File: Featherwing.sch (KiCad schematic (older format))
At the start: 21 parts, among them J2 CONN_01X16, J3 CONN_01X12, J5 GROVE-CONNECTOR-SMD-90D(4+2P-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, J9 CONN_01X06, U2 ROF-78E

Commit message: Added more signals to JST connector including DMA
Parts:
- J9: footprint Connectors_JST:JST_PH_B6B-PH-SM4-TB_06x2.00mm_Straight -> Connectors_JST:JST_PH_S6B-PH-SM4-TB_06x2.00mm_Angled
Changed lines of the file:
@@
 F 0 "J9" H 3519 3925 50  0000 C CNN
 F 1 "CONN_01X06" H 3519 4016 50  0000 C CNN
-F 2 "Connectors_JST:JST_PH_B6B-PH-SM4-TB_06x2.00mm_Straight" H 0   -150 50  0001 C CNN
+F 2 "Connectors_JST:JST_PH_S6B-PH-SM4-TB_06x2.00mm_Angled" H 0   -150 50  0001 C CNN
 F 3 "" H 0   -150 50  0001 C CNN
 	1    3600 4400

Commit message: Added PM0,1 and Deepsleep circuits
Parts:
- J9: footprint Connectors_JST:JST_PH_S6B-PH-SM4-TB_06x2.00mm_Angled -> Connectors_JST:JST_SH_SM06B-SRSS-TB_06x1.00mm_Angled
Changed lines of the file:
@@
 LIBS:logo
 LIBS:mechanical
+LIBS:whatnick
 LIBS:V9203_Devkit-cache
 EELAYER 26 0
@@
 UC
 $Comp
-L GND #PWR019
+L GND #PWR022
 U 1 1 58E27B40
 P 6800 3500
-F 0 "#PWR019" H 6850 3550 50  0001 C CNN
+F 0 "#PWR022" H 6850 3550 50  0001 C CNN
 F 1 "GND" H 6805 3327 50  0000 C CNN
 F 2 "" H 100 -150 50  0001 C CNN
@@
 $EndComp
 $Comp
-L GND #PWR020
+L GND #PWR023
 U 1 1 58E27FEA
 P 3600 3600
-F 0 "#PWR020" H 3650 3650 50  0001 C CNN
+F 0 "#PWR023" H 3650 3650 50  0001 C CNN
 F 1 "GND" H 3605 3427 50  0000 C CNN
 F 2 "" H -3100 -50 50  0001 C CNN
@@
 F 0 "J9" H 3519 3925 50  0000 C CNN
 F 1 "CONN_01X06" H 3519 4016 50  0000 C CNN
-F 2 "Connectors_JST:JST_PH_S6B-PH-SM4-TB_06x2.00mm_Angled" H 0   -150 50  0001 C CNN
+F 2 "Connectors_JST:JST_SH_SM06B-SRSS-TB_06x1.00mm_Angled" H 0   -150 50  0001 C CNN
 F 3 "" H 0   -150 50  0001 C CNN
 	1    3600 4400

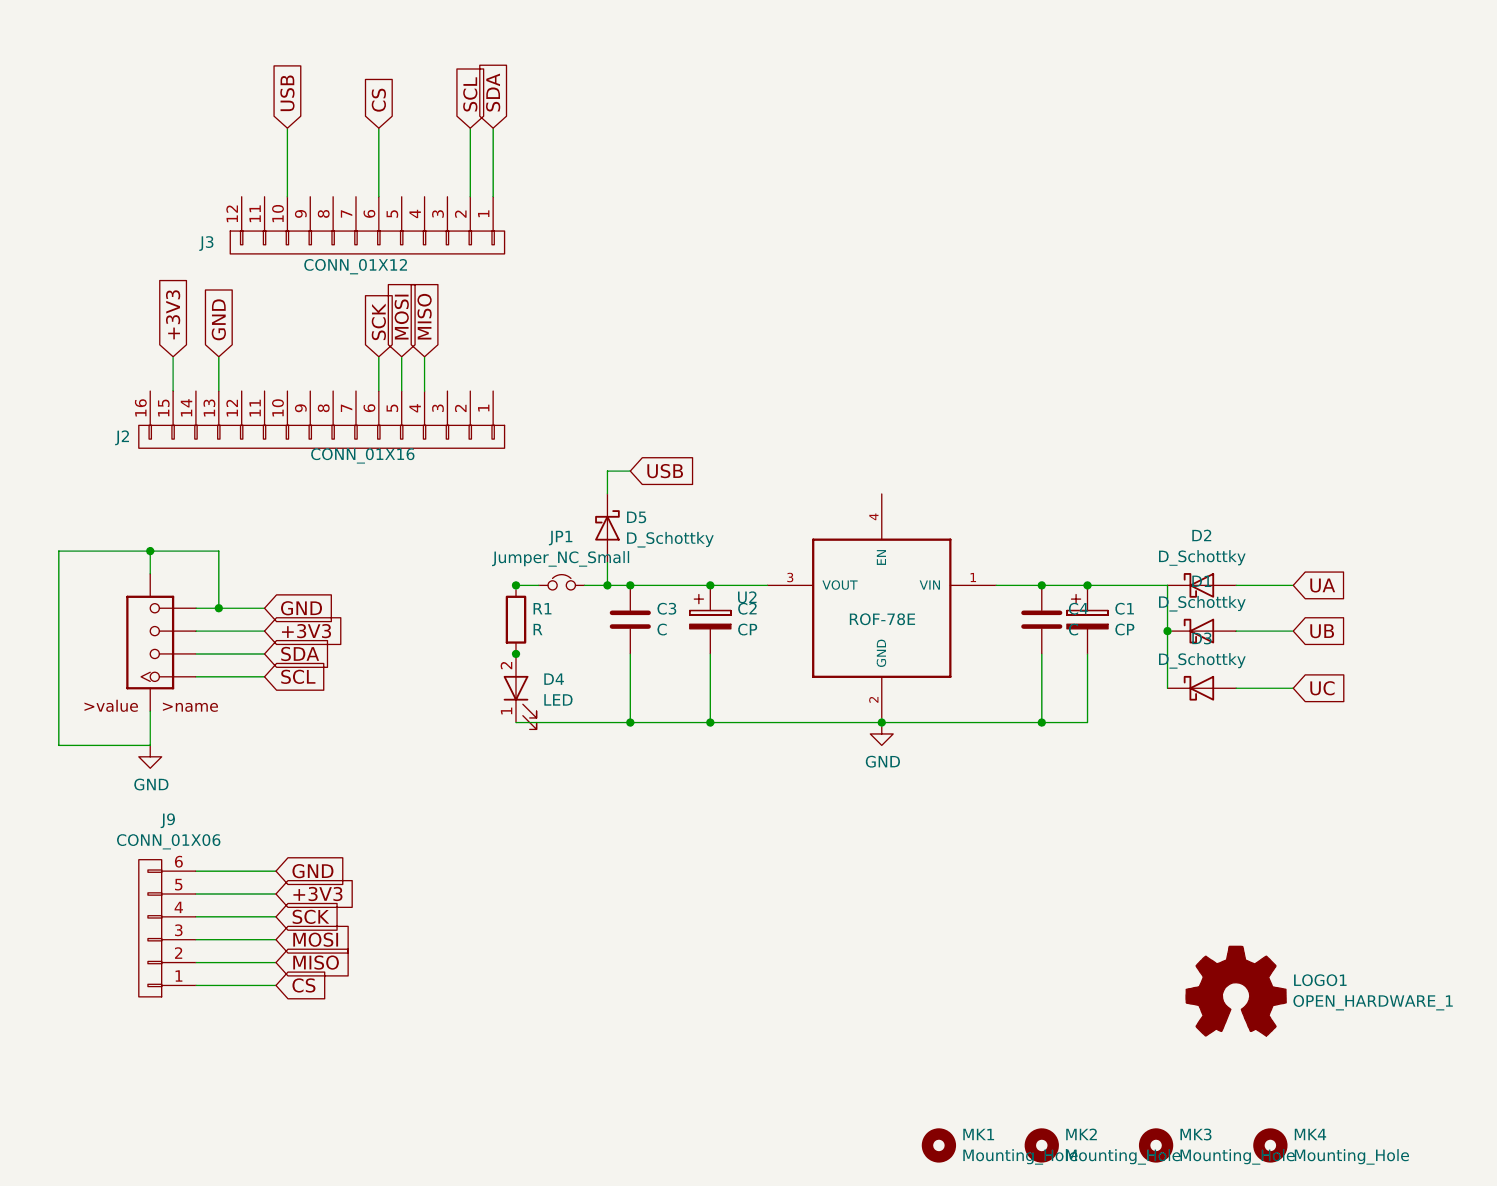
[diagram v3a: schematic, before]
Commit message: Ran ERC and updated pcb
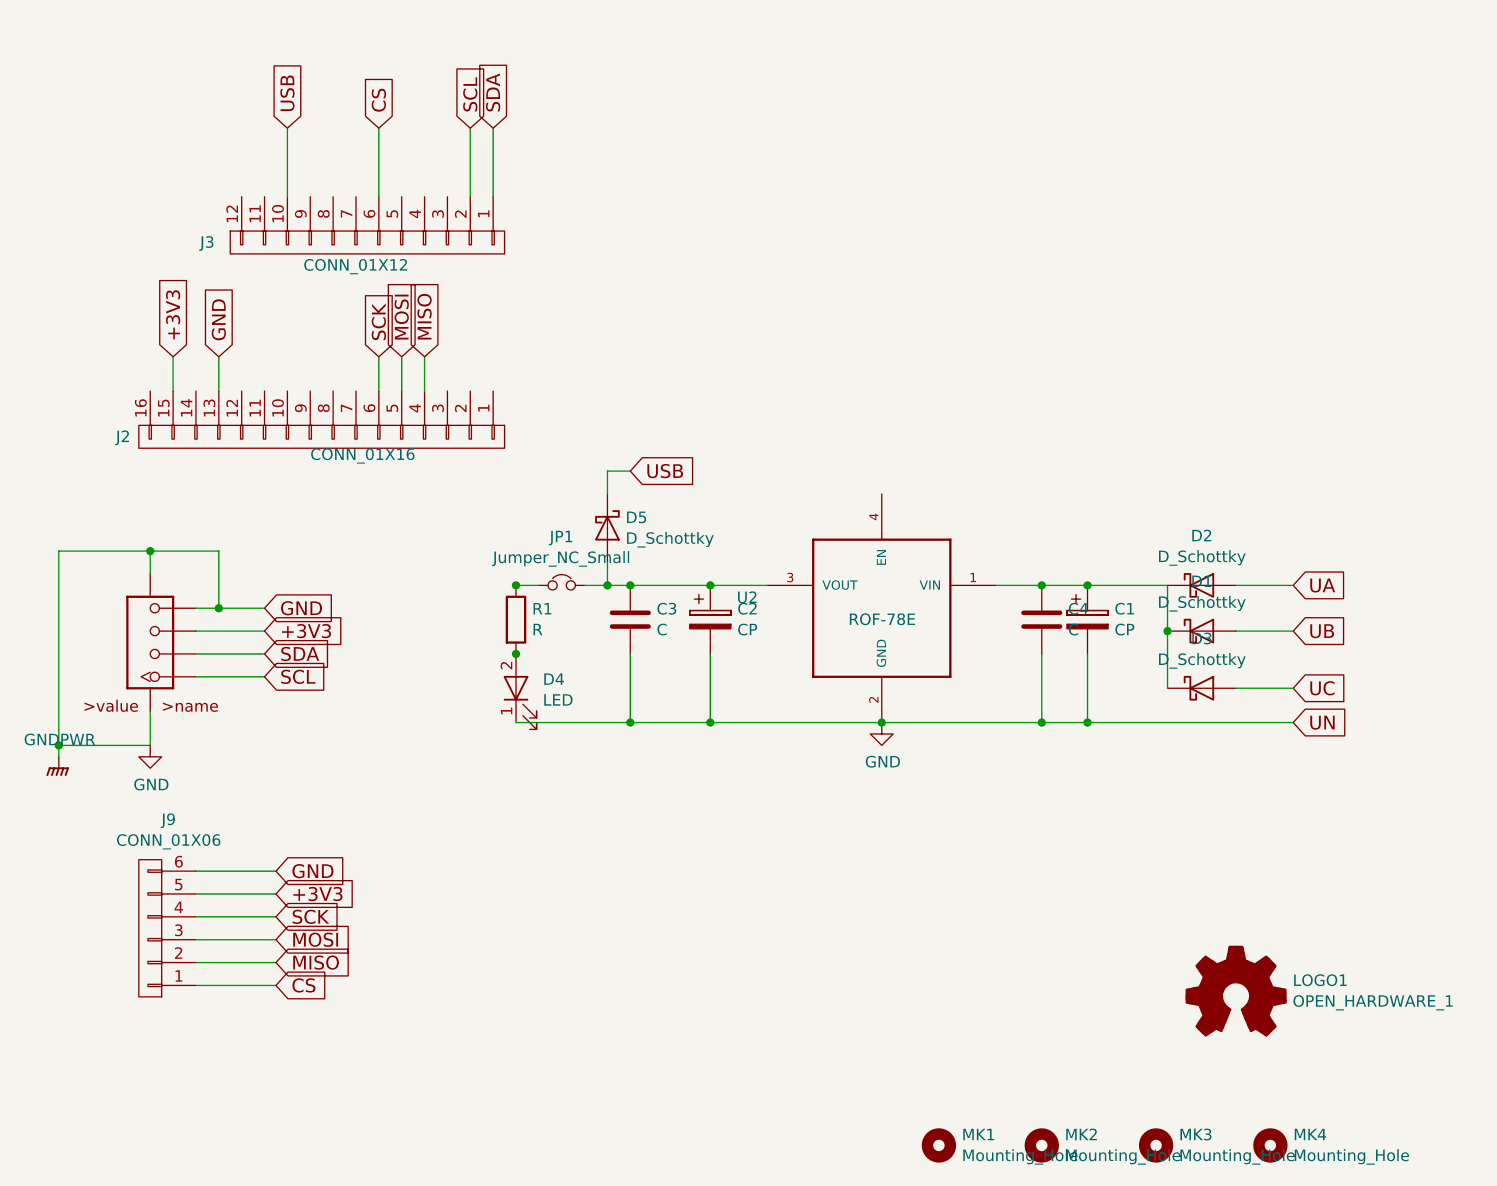
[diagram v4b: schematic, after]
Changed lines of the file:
@@
 UC
 $Comp
-L GND #PWR18
+L GND #PWR021
 U 1 1 58E27B40
 P 6800 3500
-F 0 "#PWR18" H 6850 3550 50  0001 C CNN
+F 0 "#PWR021" H 6850 3550 50  0001 C CNN
 F 1 "GND" H 6805 3327 50  0000 C CNN
 F 2 "" H 100 -150 50  0001 C CNN
@@
 $EndComp
 $Comp
-L GND #PWR17
+L GND #PWR022
 U 1 1 58E27FEA
 P 3600 3600
-F 0 "#PWR17" H 3650 3650 50  0001 C CNN
+F 0 "#PWR022" H 3650 3650 50  0001 C CNN
 F 1 "GND" H 3605 3427 50  0000 C CNN
 F 2 "" H -3100 -50 50  0001 C CNN
@@
 Connection ~ 5200 3200
 Wire Wire Line
-	5200 3500 7700 3500
+	5200 3500 8600 3500
 Connection ~ 5700 3500
 Wire Wire Line
@@
 	3600 3600 3200 3600
 Wire Wire Line
-	3200 3600 3200 2750
+	3200 2750 3200 3650
 Wire Wire Line
 	3200 2750 3900 2750
@@
 	1    0    0    -1
 $EndComp
+Connection ~ 7700 3500
+Text GLabel 8600 3500 2    60   Input ~ 0
+UN
+$Comp
+L GNDPWR #PWR023
+U 1 1 59063ED3
+P 3200 3650
+F 0 "#PWR023" H -750 -200 50  0001 C CNN
+F 1 "GNDPWR" H 3204 3724 50  0000 C CNN
+F 2 "" H -750 -50 50  0001 C CNN
+F 3 "" H -750 -50 50  0001 C CNN
+	1    3200 3650
+	1    0    0    -1
+$EndComp
+Connection ~ 3200 3600
 $EndSCHEMATC

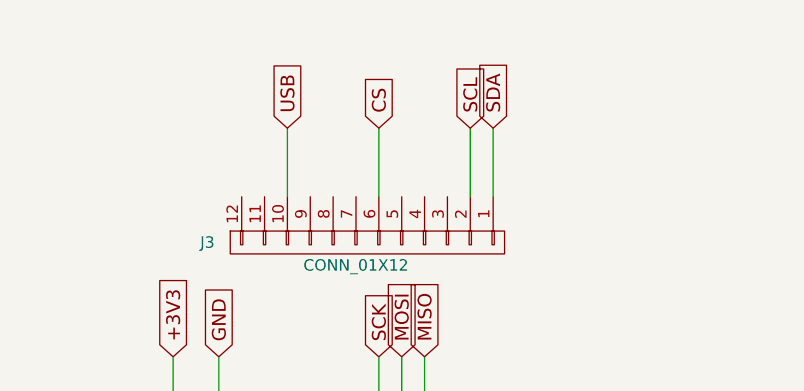
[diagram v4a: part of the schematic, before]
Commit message: With CS mux, improve silk screen in next rev
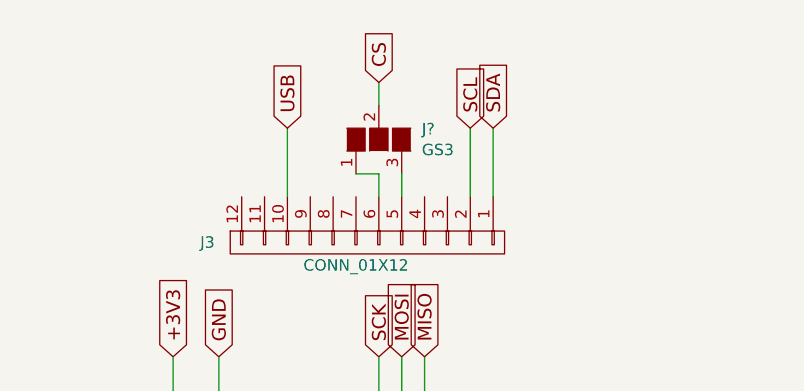
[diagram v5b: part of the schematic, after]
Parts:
- added J?: GS3, Connectors:GS3, symbol GS3
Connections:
- net CS: now also J?.2 (G2); no longer J3.6 (P6)
- net at J3.5 (P5): now also J?.3 (G3)
- new net: J3.6 (P6), J?.1 (G1)
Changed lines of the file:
@@
 Text GLabel 5700 2400 2    60   Input ~ 0
 USB
-Wire Wire Line
-	3800 3100 4100 3100
-Wire Wire Line
-	3800 3000 4100 3000
-Wire Wire Line
-	5000 1200 5000 900
-Wire Wire Line
-	5100 1200 5100 900
-Wire Wire Line
-	4200 1200 4200 900
-Connection ~ 5200 2900
-Connection ~ 5200 3200
-Wire Wire Line
-	5200 3500 8600 3500
-Connection ~ 5700 3500
-Wire Wire Line
-	5300 2900 5200 2900
-Connection ~ 5600 2900
-Connection ~ 5700 2900
-Wire Wire Line
-	5600 2900 5600 2800
-Connection ~ 6050 3500
-Wire Wire Line
-	6050 3500 6050 3200
-Connection ~ 6800 3500
-Wire Wire Line
-	5700 3200 5700 3500
-Connection ~ 6050 2900
-Wire Wire Line
-	5500 2900 6300 2900
-Connection ~ 7500 2900
-Connection ~ 7500 3500
-Wire Wire Line
-	7500 3200 7500 3500
-Wire Wire Line
-	7700 3500 7700 3200
-Connection ~ 7700 2900
-Wire Wire Line
-	7300 2900 8050 2900
-Wire Wire Line
-	8350 2900 8600 2900
-Wire Wire Line
-	8350 3100 8600 3100
-Wire Wire Line
-	8350 3350 8600 3350
-Connection ~ 8050 3100
-Wire Wire Line
-	8050 2900 8050 3350
-Wire Wire Line
-	3800 3200 4100 3200
-Wire Wire Line
-	3800 3300 4100 3300
-Wire Wire Line
-	3600 3450 3600 3600
-Wire Wire Line
-	3600 3600 3200 3600
-Wire Wire Line
-	3200 2750 3200 3650
-Wire Wire Line
-	3200 2750 3900 2750
-Wire Wire Line
-	3600 2750 3600 2850
-Wire Wire Line
-	3900 2750 3900 3000
-Connection ~ 3900 3000
-Connection ~ 3600 2750
-Wire Wire Line
-	5600 2500 5600 2400
-Wire Wire Line
-	5600 2400 5700 2400
-Wire Wire Line
-	3700 2050 3700 1900
-Wire Wire Line
-	3900 2050 3900 1900
-Wire Wire Line
-	4800 2050 4800 1900
-Wire Wire Line
-	4700 2050 4700 1900
-Wire Wire Line
-	4600 2050 4600 1900
 Text GLabel 3700 1900 1    60   Input ~ 0
 +3V3
@@
 Text GLabel 4800 1900 1    60   Input ~ 0
 MISO
-Wire Wire Line
-	4600 1200 4600 900
-Text GLabel 4600 900  1    60   Input ~ 0
+Text GLabel 4600 700  1    60   Input ~ 0
 CS
 $Comp
@@
 	-1   0    0    1
 $EndComp
-Wire Wire Line
-	3800 4150 4150 4150
-Wire Wire Line
-	3800 4250 4150 4250
-Wire Wire Line
-	3800 4350 4150 4350
-Wire Wire Line
-	3800 4450 4150 4450
-Wire Wire Line
-	3800 4550 4150 4550
-Wire Wire Line
-	3800 4650 4150 4650
 Text GLabel 4150 4150 2    60   Input ~ 0
 GND
@@
 	1    0    0    -1
 $EndComp
-Connection ~ 7700 3500
 Text GLabel 8600 3500 2    60   Input ~ 0
 UN
@@
 	1    0    0    -1
 $EndComp
+$Comp
+L GS3 J?
+U 1 1 59075259
+P 4600 950
+F 0 "J?" V 4646 762 50  0000 R CNN
+F 1 "GS3" V 4555 762 50  0000 R CNN
+F 2 "Connectors:GS3" V 88  -174 50  0001 C CNN
+F 3 "" H 0   -100 50  0001 C CNN
+	1    4600 950
+	0    -1   -1   0
+$EndComp
+Wire Wire Line
+	4600 700  4600 800
 Connection ~ 3200 3600
+Connection ~ 7700 3500
+Wire Wire Line
+	3800 4650 4150 4650
+Wire Wire Line
+	3800 4550 4150 4550
+Wire Wire Line
+	3800 4450 4150 4450
+Wire Wire Line
+	3800 4350 4150 4350
+Wire Wire Line
+	3800 4250 4150 4250
+Wire Wire Line
+	3800 4150 4150 4150
+Wire Wire Line
+	4600 2050 4600 1900
+Wire Wire Line
+	4700 2050 4700 1900
+Wire Wire Line
+	4800 2050 4800 1900
+Wire Wire Line
+	3900 2050 3900 1900
+Wire Wire Line
+	3700 2050 3700 1900
+Wire Wire Line
+	5600 2400 5700 2400
+Wire Wire Line
+	5600 2500 5600 2400
+Connection ~ 3600 2750
+Connection ~ 3900 3000
+Wire Wire Line
+	3900 2750 3900 3000
+Wire Wire Line
+	3600 2750 3600 2850
+Wire Wire Line
+	3200 2750 3900 2750
+Wire Wire Line
+	3200 2750 3200 3650
+Wire Wire Line
+	3600 3600 3200 3600
+Wire Wire Line
+	3600 3450 3600 3600
+Wire Wire Line
+	3800 3300 4100 3300
+Wire Wire Line
+	3800 3200 4100 3200
+Wire Wire Line
+	8050 2900 8050 3350
+Connection ~ 8050 3100
+Wire Wire Line
+	8350 3350 8600 3350
+Wire Wire Line
+	8350 3100 8600 3100
+Wire Wire Line
+	8350 2900 8600 2900
+Wire Wire Line
+	7300 2900 8050 2900
+Connection ~ 7700 2900
+Wire Wire Line
+	7700 3500 7700 3200
+Wire Wire Line
+	7500 3200 7500 3500
+Connection ~ 7500 3500
+Connection ~ 7500 2900
+Wire Wire Line
+	5500 2900 6300 2900
+Connection ~ 6050 2900
+Wire Wire Line
+	5700 3200 5700 3500
+Connection ~ 6800 3500
+Wire Wire Line
+	6050 3500 6050 3200
+Connection ~ 6050 3500
+Wire Wire Line
+	5600 2900 5600 2800
+Connection ~ 5700 2900
+Connection ~ 5600 2900
+Wire Wire Line
+	5300 2900 5200 2900
+Connection ~ 5700 3500
+Wire Wire Line
+	5200 3500 8600 3500
+Connection ~ 5200 3200
+Connection ~ 5200 2900
+Wire Wire Line
+	4200 1200 4200 900
+Wire Wire Line
+	5100 1200 5100 900
+Wire Wire Line
+	5000 1200 5000 900
+Wire Wire Line
+	3800 3000 4100 3000
+Wire Wire Line
+	3800 3100 4100 3100
+Wire Wire Line
+	4500 1100 4600 1100
+Wire Wire Line
+	4600 1100 4600 1200
+Wire Wire Line
+	4700 1100 4700 1200
 $EndSCHEMATC

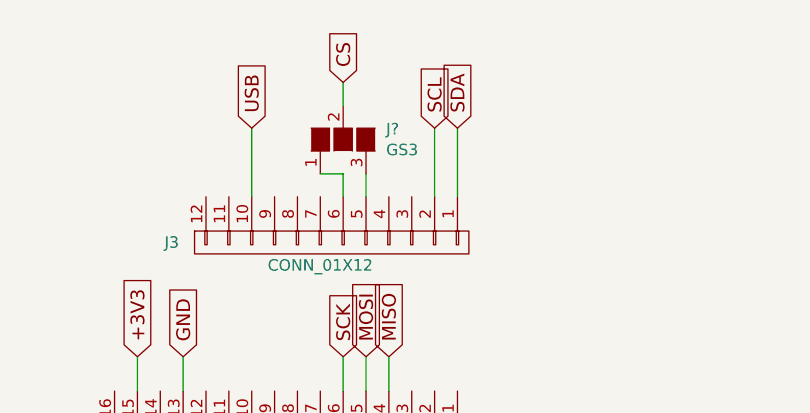
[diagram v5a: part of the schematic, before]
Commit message: Added silk screen markers
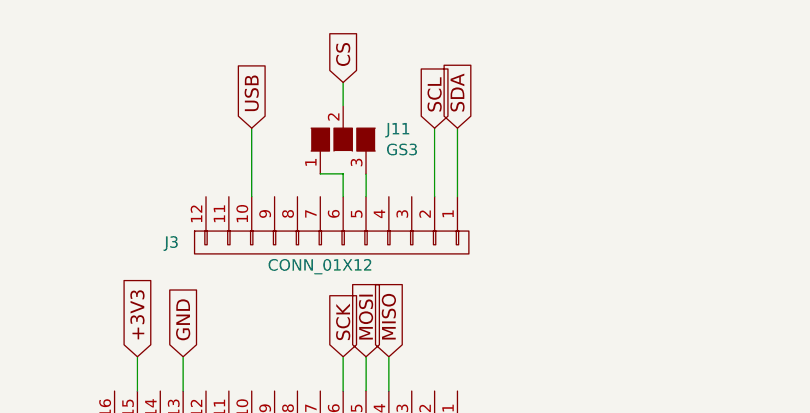
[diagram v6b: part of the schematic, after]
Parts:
- J11: renamed from J?; footprint Connectors:GS3 -> Connect:GS3
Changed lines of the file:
@@
 $EndComp
 $Comp
-L GS3 J?
+L GS3 J11
 U 1 1 59075259
 P 4600 950
-F 0 "J?" V 4646 762 50  0000 R CNN
+F 0 "J11" V 4646 762 50  0000 R CNN
 F 1 "GS3" V 4555 762 50  0000 R CNN
-F 2 "Connectors:GS3" V 88  -174 50  0001 C CNN
+F 2 "Connect:GS3" V 88  -174 50  0001 C CNN
 F 3 "" H 0   -100 50  0001 C CNN
 	1    4600 950
